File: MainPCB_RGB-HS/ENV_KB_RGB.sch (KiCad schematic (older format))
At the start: 297 parts

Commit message: Generated JLCPCB Compatible Gerber, BOM and CPL for HS/RGB Version
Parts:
- PowerLedResistor0: value 1K Resistor 0402 -> 2.2K Resistor 0402
- SW-RST0: value B3U-1000 -> B3U
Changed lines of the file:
@@
 P 8550 9950
 F 0 "PowerLedResistor0" V 8650 10200 50  0000 C CNN
-F 1 "1K Resistor 0402" V 8700 10000 50  0001 C CNN
+F 1 "2.2K Resistor 0402" V 8700 10000 50  0001 C CNN
 F 2 "Resistor_SMD:R_0402_1005Metric" H 8550 9950 50  0001 C CNN
 F 3 "~" H 8550 9950 50  0001 C CNN
@@
 P 8550 10700
 F 0 "SW-RST0" H 8550 11100 50  0000 C CNN
-F 1 "B3U-1000" H 8550 10950 50  0000 C CNN
+F 1 "B3U" H 8550 10950 50  0000 C CNN
 F 2 "Button_Switch_SMD:SW_SPST_B3U-1000P" H 8550 10700 50  0001 L BNN
 F 3 "" H 8550 10700 50  0001 L BNN

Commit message: shrunk the PCBs width down to 347mm to comply with JLCPCBs max size for 4 layers.
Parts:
- H0, H1, H10, H3, H4, H6, H7, H9: symbol Mechanical:MountingHole -> Mechanical:MountingHole_Pad
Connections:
- net GND: now also H0.1, H1.1, H10.1, H3.1, H4.1, H6.1, H7.1, H9.1
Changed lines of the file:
@@
 This needs double checking
 $Comp
-L Mechanical:MountingHole H9
+L Mechanical:MountingHole_Pad H9
 U 1 1 60717F95
 P 6600 10650
@@
 $EndComp
 $Comp
-L Mechanical:MountingHole H10
+L Mechanical:MountingHole_Pad H10
 U 1 1 607429B3
-P 6600 10850
-F 0 "H10" H 6700 10896 50  0000 L CNN
-F 1 "MountingHole" H 6700 10805 50  0000 L CNN
-F 2 "MountingHole:MountingHole_2.2mm_M2_Pad" H 6600 10850 50  0001 C CNN
-F 3 "~" H 6600 10850 50  0001 C CNN
-	1    6600 10850
+P 6800 10650
+F 0 "H10" H 6900 10696 50  0000 L CNN
+F 1 "MountingHole" H 6900 10605 50  0000 L CNN
+F 2 "MountingHole:MountingHole_2.2mm_M2_Pad" H 6800 10650 50  0001 C CNN
+F 3 "~" H 6800 10650 50  0001 C CNN
+	1    6800 10650
 	1    0    0    -1
 $EndComp
@@
 GND
 $Comp
-L Mechanical:MountingHole H7
+L Mechanical:MountingHole_Pad H7
 U 1 1 6077360A
-P 6600 10250
-F 0 "H7" H 6700 10296 50  0000 L CNN
-F 1 "MountingHole" H 6700 10205 50  0000 L CNN
-F 2 "MountingHole:MountingHole_2.2mm_M2_Pad" H 6600 10250 50  0001 C CNN
-F 3 "~" H 6600 10250 50  0001 C CNN
-	1    6600 10250
-	1    0    0    -1
-$EndComp
-$Comp
-L Mechanical:MountingHole H6
+P 6400 10650
+F 0 "H7" H 6500 10696 50  0000 L CNN
+F 1 "MountingHole" H 6500 10605 50  0000 L CNN
+F 2 "MountingHole:MountingHole_2.2mm_M2_Pad" H 6400 10650 50  0001 C CNN
+F 3 "~" H 6400 10650 50  0001 C CNN
+	1    6400 10650
+	1    0    0    -1
+$EndComp
+$Comp
+L Mechanical:MountingHole_Pad H6
 U 1 1 60748B43
-P 6600 10050
-F 0 "H6" H 6700 10096 50  0000 L CNN
-F 1 "MountingHole" H 6700 10005 50  0000 L CNN
-F 2 "MountingHole:MountingHole_2.2mm_M2_Pad" H 6600 10050 50  0001 C CNN
-F 3 "~" H 6600 10050 50  0001 C CNN
-	1    6600 10050
-	1    0    0    -1
-$EndComp
-$Comp
-L Mechanical:MountingHole H4
+P 6200 10650
+F 0 "H6" H 6300 10696 50  0000 L CNN
+F 1 "MountingHole" H 6300 10605 50  0000 L CNN
+F 2 "MountingHole:MountingHole_2.2mm_M2_Pad" H 6200 10650 50  0001 C CNN
+F 3 "~" H 6200 10650 50  0001 C CNN
+	1    6200 10650
+	1    0    0    -1
+$EndComp
+$Comp
+L Mechanical:MountingHole_Pad H4
 U 1 1 6068A680
-P 6600 9650
-F 0 "H4" H 6700 9696 50  0000 L CNN
-F 1 "MountingHole" H 6700 9605 50  0000 L CNN
-F 2 "MountingHole:MountingHole_2.2mm_M2_Pad" H 6600 9650 50  0001 C CNN
-F 3 "~" H 6600 9650 50  0001 C CNN
-	1    6600 9650
-	1    0    0    -1
-$EndComp
-$Comp
-L Mechanical:MountingHole H1
+P 6000 10650
+F 0 "H4" H 6100 10696 50  0000 L CNN
+F 1 "MountingHole" H 6100 10605 50  0000 L CNN
+F 2 "MountingHole:MountingHole_2.2mm_M2_Pad" H 6000 10650 50  0001 C CNN
+F 3 "~" H 6000 10650 50  0001 C CNN
+	1    6000 10650
+	1    0    0    -1
+$EndComp
+$Comp
+L Mechanical:MountingHole_Pad H1
 U 1 1 605BD366
-P 6600 9050
-F 0 "H1" H 6700 9096 50  0000 L CNN
-F 1 "MountingHole" H 6700 9005 50  0000 L CNN
-F 2 "MountingHole:MountingHole_2.2mm_M2_Pad" H 6600 9050 50  0001 C CNN
-F 3 "~" H 6600 9050 50  0001 C CNN
-	1    6600 9050
-	1    0    0    -1
-$EndComp
-$Comp
-L Mechanical:MountingHole H3
+P 5600 10650
+F 0 "H1" H 5700 10696 50  0000 L CNN
+F 1 "MountingHole" H 5700 10605 50  0000 L CNN
+F 2 "MountingHole:MountingHole_2.2mm_M2_Pad" H 5600 10650 50  0001 C CNN
+F 3 "~" H 5600 10650 50  0001 C CNN
+	1    5600 10650
+	1    0    0    -1
+$EndComp
+$Comp
+L Mechanical:MountingHole_Pad H3
 U 1 1 6058BC08
-P 6600 9450
-F 0 "H3" H 6700 9496 50  0000 L CNN
-F 1 "MountingHole" H 6700 9405 50  0000 L CNN
-F 2 "MountingHole:MountingHole_2.2mm_M2_Pad" H 6600 9450 50  0001 C CNN
-F 3 "~" H 6600 9450 50  0001 C CNN
-	1    6600 9450
-	1    0    0    -1
-$EndComp
-$Comp
-L Mechanical:MountingHole H0
+P 5800 10650
+F 0 "H3" H 5900 10696 50  0000 L CNN
+F 1 "MountingHole" H 5900 10605 50  0000 L CNN
+F 2 "MountingHole:MountingHole_2.2mm_M2_Pad" H 5800 10650 50  0001 C CNN
+F 3 "~" H 5800 10650 50  0001 C CNN
+	1    5800 10650
+	1    0    0    -1
+$EndComp
+$Comp
+L Mechanical:MountingHole_Pad H0
 U 1 1 605938C3
-P 6600 8850
-F 0 "H0" H 6700 8896 50  0000 L CNN
-F 1 "MountingHole" H 6700 8805 50  0000 L CNN
-F 2 "MountingHole:MountingHole_2.2mm_M2_Pad" H 6600 8850 50  0001 C CNN
-F 3 "~" H 6600 8850 50  0001 C CNN
-	1    6600 8850
+P 5400 10650
+F 0 "H0" H 5500 10696 50  0000 L CNN
+F 1 "MountingHole" H 5500 10605 50  0000 L CNN
+F 2 "MountingHole:MountingHole_2.2mm_M2_Pad" H 5400 10650 50  0001 C CNN
+F 3 "~" H 5400 10650 50  0001 C CNN
+	1    5400 10650
 	1    0    0    -1
 $EndComp
@@
 Wire Wire Line
 	30200 3500 30250 3500
+Wire Wire Line
+	5400 10750 5600 10750
+Connection ~ 5600 10750
+Wire Wire Line
+	5600 10750 5800 10750
+Connection ~ 5800 10750
+Wire Wire Line
+	5800 10750 6000 10750
+Connection ~ 6000 10750
+Wire Wire Line
+	6000 10750 6200 10750
+Connection ~ 6200 10750
+Wire Wire Line
+	6200 10750 6400 10750
+Connection ~ 6400 10750
+Wire Wire Line
+	6400 10750 6600 10750
+Connection ~ 6600 10750
+Wire Wire Line
+	6600 10750 6800 10750
+Wire Wire Line
+	6800 10750 6800 11000
+Connection ~ 6800 10750
+Text GLabel 6800 11000 2    50   Input ~ 0
+GND
 $EndSCHEMATC

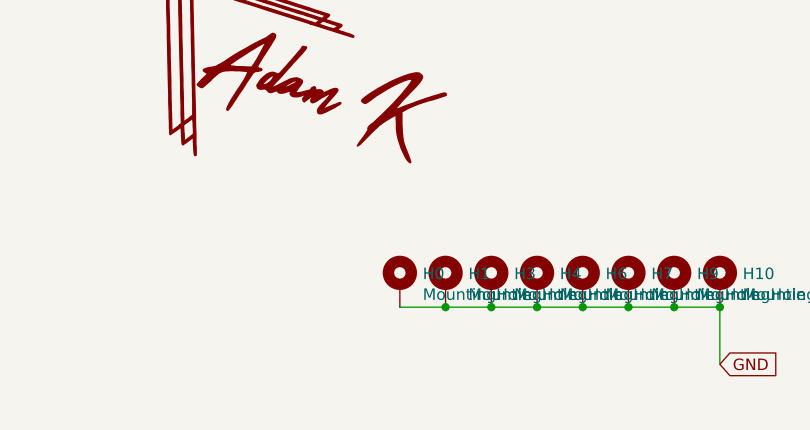
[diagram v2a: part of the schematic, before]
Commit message: Modified RGB/HS to be less wide so you can have it made via JLCPCB, Also made new logo and name for this version.
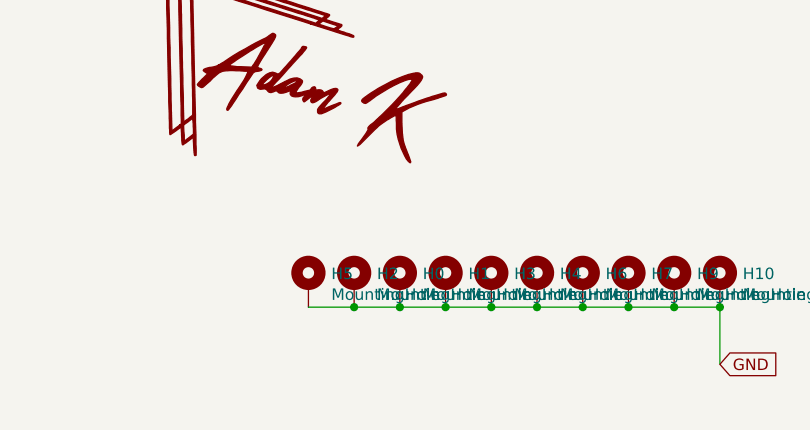
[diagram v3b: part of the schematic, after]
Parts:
- added H2, H5: MountingHole, MountingHole:MountingHole_2.2mm_M2_Pad, symbol Mechanical:MountingHole_Pad
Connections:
- net GND: now also H2.1, H5.1
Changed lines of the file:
@@
 Text GLabel 6800 11000 2    50   Input ~ 0
 GND
+$Comp
+L Mechanical:MountingHole_Pad H2
+U 1 1 61411D60
+P 5200 10650
+F 0 "H2" H 5300 10696 50  0000 L CNN
+F 1 "MountingHole" H 5300 10605 50  0000 L CNN
+F 2 "MountingHole:MountingHole_2.2mm_M2_Pad" H 5200 10650 50  0001 C CNN
+F 3 "~" H 5200 10650 50  0001 C CNN
+	1    5200 10650
+	1    0    0    -1
+$EndComp
+Wire Wire Line
+	5200 10750 5400 10750
+Connection ~ 5400 10750
+$Comp
+L Mechanical:MountingHole_Pad H5
+U 1 1 6162A1BF
+P 5000 10650
+F 0 "H5" H 5100 10696 50  0000 L CNN
+F 1 "MountingHole" H 5100 10605 50  0000 L CNN
+F 2 "MountingHole:MountingHole_2.2mm_M2_Pad" H 5000 10650 50  0001 C CNN
+F 3 "~" H 5000 10650 50  0001 C CNN
+	1    5000 10650
+	1    0    0    -1
+$EndComp
+Wire Wire Line
+	5000 10750 5200 10750
+Connection ~ 5200 10750
 $EndSCHEMATC

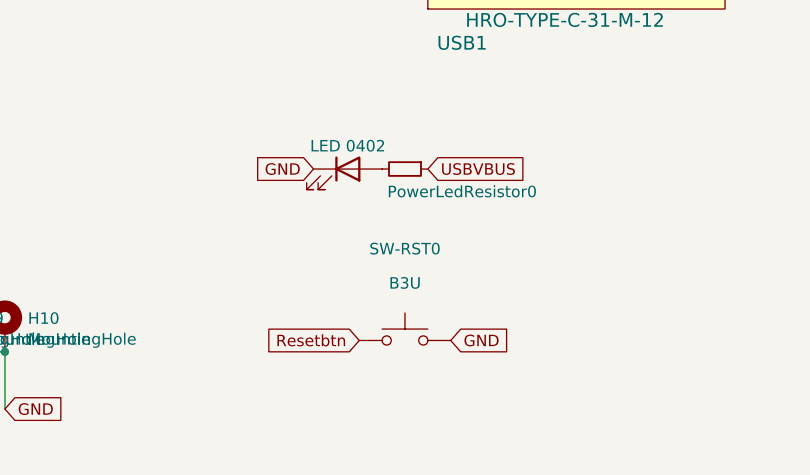
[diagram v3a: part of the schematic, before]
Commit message: updated PCB to have through hole parts except type-c port.
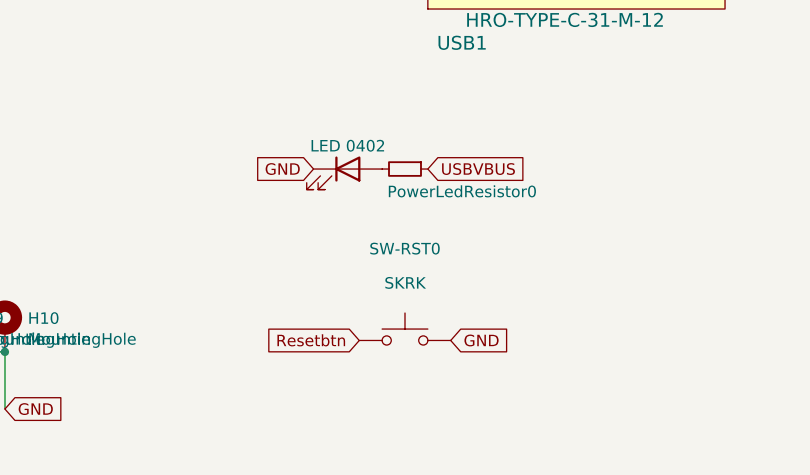
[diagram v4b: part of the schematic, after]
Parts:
- PowerLED0: footprint LED_SMD:LED_0402_1005Metric -> LED_THT:LED_D3.0mm
- PowerLedResistor0, RESISTOR0, RESISTOR1: footprint Resistor_SMD:R_0402_1005Metric -> Resistor_THT:R_Axial_DIN0204_L3.6mm_D1.6mm_P5.08mm_Horizontal
- SW-RST0: value B3U -> SKRK; footprint Button_Switch_SMD:SW_SPST_B3U-1000P -> Button_Switch_SMD:SW_Push_SPST_NO_Alps_SKRK
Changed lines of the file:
@@
 F 0 "RESISTOR1" V 8804 8600 39  0001 C CNN
 F 1 "5.1kohm 0402" V 9000 8700 30  0001 C CNN
-F 2 "Resistor_SMD:R_0402_1005Metric" H 9000 8600 50  0001 C CNN
+F 2 "Resistor_THT:R_Axial_DIN0204_L3.6mm_D1.6mm_P5.08mm_Horizontal" H 9000 8600 50  0001 C CNN
 F 3 "~" H 9000 8600 50  0001 C CNN
 F 4 "C25905" V 9000 8600 50  0001 C CNN "LCSC"
@@
 F 0 "RESISTOR0" V 9404 8600 39  0001 C CNN
 F 1 "5.1kohm 0402" V 9495 8600 50  0001 C CNN
-F 2 "Resistor_SMD:R_0402_1005Metric" H 9600 8600 50  0001 C CNN
+F 2 "Resistor_THT:R_Axial_DIN0204_L3.6mm_D1.6mm_P5.08mm_Horizontal" H 9600 8600 50  0001 C CNN
 F 3 "~" H 9600 8600 50  0001 C CNN
 F 4 "C25905" V 9600 8600 50  0001 C CNN "LCSC"
@@
 F 0 "PowerLED0" H 8293 10167 50  0001 C CNN
 F 1 "LED 0402" H 8300 10050 50  0000 C CNN
-F 2 "LED_SMD:LED_0402_1005Metric" H 8300 9950 50  0001 C CNN
+F 2 "LED_THT:LED_D3.0mm" H 8300 9950 50  0001 C CNN
 F 3 "~" H 8300 9950 50  0001 C CNN
 	1    8300 9950
@@
 F 0 "PowerLedResistor0" V 8650 10200 50  0000 C CNN
 F 1 "2.2K Resistor 0402" V 8700 10000 50  0001 C CNN
-F 2 "Resistor_SMD:R_0402_1005Metric" H 8550 9950 50  0001 C CNN
+F 2 "Resistor_THT:R_Axial_DIN0204_L3.6mm_D1.6mm_P5.08mm_Horizontal" H 8550 9950 50  0001 C CNN
 F 3 "~" H 8550 9950 50  0001 C CNN
 F 4 "C17513" V 8550 9950 50  0001 C CNN "LCSC"
@@
 P 8550 10700
 F 0 "SW-RST0" H 8550 11100 50  0000 C CNN
-F 1 "B3U" H 8550 10950 50  0000 C CNN
-F 2 "Button_Switch_SMD:SW_SPST_B3U-1000P" H 8550 10700 50  0001 L BNN
+F 1 "SKRK" H 8550 10950 50  0000 C CNN
+F 2 "Button_Switch_SMD:SW_Push_SPST_NO_Alps_SKRK" H 8550 10700 50  0001 L BNN
 F 3 "" H 8550 10700 50  0001 L BNN
 F 4 "Omron" H 8550 10700 50  0001 L BNN "MANUFACTURER"

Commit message: some more general re-working of HS/RGB version
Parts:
- added Stab1: Stabilizer, Mounting_Keyboard_Stabilizer:Stabilizer_Cherry_MX_6.25u, symbol Mechanical:MountingHole
- added Stab2, Stab3, Stab4: Stabilizer, Mounting_Keyboard_Stabilizer:Stabilizer_Cherry_MX_2u, symbol Mechanical:MountingHole
- K_0, K_1, K_10, K_11, K_12, K_13, K_14, K_15, K_16, K_17, K_18, K_19, K_2, K_20, K_21, K_22, K_23, K_24, K_25, K_26, K_27, K_28, K_3, K_30, K_31, K_32, K_34, K_35, K_36, K_37, K_38, K_39, K_4, K_40, K_41, K_42, K_43, K_44, K_45, K_47, K_48, K_49, K_5, K_51, K_52, K_53, K_54, K_55, K_56, K_57, K_58, K_59, K_6, K_60, K_61, K_62, K_65, K_66, K_67, K_68, K_69, K_7, K_70, K_71, K_72, K_73, K_74, K_75, K_77, K_8, K_86, K_87, K_88, K_9: footprint MX_Only:MXOnly-1U-Hotswap -> MX_Only:MXOnly-1U-Hotswap-Modified
- K_29, K_63: footprint MX_Only:MXOnly-2U-Hotswap -> MX_Only:MXOnly-1U-Hotswap-Modified
- K_33, K_46: footprint MX_Only:MXOnly-1.5U-Hotswap -> MX_Only:MXOnly-1U-Hotswap-Modified
- K_50: footprint MX_Only:MXOnly-1.75U-Hotswap -> MX_Only:MXOnly-1U-Hotswap-Modified
- K_63B1, K_64B1: footprint MX_Only:MXOnly-2.25U-Hotswap -> MX_Only:MXOnly-1U-Hotswap-Modified
- K_64, K_78, K_79, K_80, K_82, K_83, K_84, K_85: footprint MX_Only:MXOnly-1.25U-Hotswap -> MX_Only:MXOnly-1U-Hotswap-Modified
- K_76: footprint MX_Only:MXOnly-2.75U-Hotswap -> MX_Only:MXOnly-1U-Hotswap-Modified
- K_81: footprint MX_Only:MXOnly-6.25U-Hotswap-ReversedStabilizers -> MX_Only:MXOnly-1U-Hotswap-Modified

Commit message: generated laser cut files for current PCB version, changed footprint size of resistors to 1/4 instead of 1/8w
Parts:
- LEDRESISTOR1: renamed from PowerLedResistor0; value 2.2K Resistor 0402 -> 5.1K Resistor 1/4w; footprint Resistor_THT:R_Axial_DIN0204_L3.6mm_D1.6mm_P5.08mm_Horizontal -> Resistor_THT:R_Axial_DIN0204_L3.6mm_D1.6mm_P7.62mm_Horizontal
- PowerLED0: value LED 0402 -> LED 3MM
- RESISTOR0: value 5.1kohm 0402 -> 5.1kohm 1/4w; footprint Resistor_THT:R_Axial_DIN0204_L3.6mm_D1.6mm_P5.08mm_Horizontal -> Resistor_THT:R_Axial_DIN0204_L3.6mm_D1.6mm_P7.62mm_Horizontal
- RESISTOR1: value 5.1kohm 0402 -> 5.1kohm 1/4; footprint Resistor_THT:R_Axial_DIN0204_L3.6mm_D1.6mm_P5.08mm_Horizontal -> Resistor_THT:R_Axial_DIN0204_L3.6mm_D1.6mm_P7.62mm_Horizontal
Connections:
- no-connect marks 0 -> 2
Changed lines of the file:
@@
 P 9000 8600
 F 0 "RESISTOR1" V 8804 8600 39  0001 C CNN
-F 1 "5.1kohm 0402" V 9000 8700 30  0001 C CNN
-F 2 "Resistor_THT:R_Axial_DIN0204_L3.6mm_D1.6mm_P5.08mm_Horizontal" H 9000 8600 50  0001 C CNN
+F 1 "5.1kohm 1/4" V 9000 8700 30  0001 C CNN
+F 2 "Resistor_THT:R_Axial_DIN0204_L3.6mm_D1.6mm_P7.62mm_Horizontal" H 9000 8600 50  0001 C CNN
 F 3 "~" H 9000 8600 50  0001 C CNN
 F 4 "C25905" V 9000 8600 50  0001 C CNN "LCSC"
@@
 P 9600 8600
 F 0 "RESISTOR0" V 9404 8600 39  0001 C CNN
-F 1 "5.1kohm 0402" V 9495 8600 50  0001 C CNN
-F 2 "Resistor_THT:R_Axial_DIN0204_L3.6mm_D1.6mm_P5.08mm_Horizontal" H 9600 8600 50  0001 C CNN
+F 1 "5.1kohm 1/4w" V 9495 8600 50  0001 C CNN
+F 2 "Resistor_THT:R_Axial_DIN0204_L3.6mm_D1.6mm_P7.62mm_Horizontal" H 9600 8600 50  0001 C CNN
 F 3 "~" H 9600 8600 50  0001 C CNN
 F 4 "C25905" V 9600 8600 50  0001 C CNN "LCSC"
@@
 P 8300 9950
 F 0 "PowerLED0" H 8293 10167 50  0001 C CNN
-F 1 "LED 0402" H 8300 10050 50  0000 C CNN
+F 1 "LED 3MM" H 8300 10050 50  0000 C CNN
 F 2 "LED_THT:LED_D3.0mm" H 8300 9950 50  0001 C CNN
 F 3 "~" H 8300 9950 50  0001 C CNN
@@
 USBVBUS
 $Comp
-L Device:R_Small PowerLedResistor0
+L Device:R_Small LEDRESISTOR1
 U 1 1 604A80B1
 P 8550 9950
-F 0 "PowerLedResistor0" V 8650 10200 50  0000 C CNN
-F 1 "2.2K Resistor 0402" V 8700 10000 50  0001 C CNN
-F 2 "Resistor_THT:R_Axial_DIN0204_L3.6mm_D1.6mm_P5.08mm_Horizontal" H 8550 9950 50  0001 C CNN
+F 0 "LEDRESISTOR1" V 8650 10200 50  0000 C CNN
+F 1 "5.1K Resistor 1/4w" V 8700 10000 50  0001 C CNN
+F 2 "Resistor_THT:R_Axial_DIN0204_L3.6mm_D1.6mm_P7.62mm_Horizontal" H 8550 9950 50  0001 C CNN
 F 3 "~" H 8550 9950 50  0001 C CNN
 F 4 "C17513" V 8550 9950 50  0001 C CNN "LCSC"
@@
 	1    0    0    1
 $EndComp
+NoConn ~ 8900 8700
+NoConn ~ 9500 8700
 $EndSCHEMATC

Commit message: Corrected resistor footprint and adjusted placement, added cutout for direct mount usb castellation.
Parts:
- LEDRESISTOR1, RESISTOR0, RESISTOR1: footprint Resistor_THT:R_Axial_DIN0204_L3.6mm_D1.6mm_P7.62mm_Horizontal -> Resistor_THT:R_Axial_DIN0207_L6.3mm_D2.5mm_P10.16mm_Horizontal
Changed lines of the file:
@@
 F 0 "RESISTOR1" V 8804 8600 39  0001 C CNN
 F 1 "5.1kohm 1/4" V 9000 8700 30  0001 C CNN
-F 2 "Resistor_THT:R_Axial_DIN0204_L3.6mm_D1.6mm_P7.62mm_Horizontal" H 9000 8600 50  0001 C CNN
+F 2 "Resistor_THT:R_Axial_DIN0207_L6.3mm_D2.5mm_P10.16mm_Horizontal" H 9000 8600 50  0001 C CNN
 F 3 "~" H 9000 8600 50  0001 C CNN
 F 4 "C25905" V 9000 8600 50  0001 C CNN "LCSC"
@@
 F 0 "RESISTOR0" V 9404 8600 39  0001 C CNN
 F 1 "5.1kohm 1/4w" V 9495 8600 50  0001 C CNN
-F 2 "Resistor_THT:R_Axial_DIN0204_L3.6mm_D1.6mm_P7.62mm_Horizontal" H 9600 8600 50  0001 C CNN
+F 2 "Resistor_THT:R_Axial_DIN0207_L6.3mm_D2.5mm_P10.16mm_Horizontal" H 9600 8600 50  0001 C CNN
 F 3 "~" H 9600 8600 50  0001 C CNN
 F 4 "C25905" V 9600 8600 50  0001 C CNN "LCSC"
@@
 F 0 "LEDRESISTOR1" V 8650 10200 50  0000 C CNN
 F 1 "5.1K Resistor 1/4w" V 8700 10000 50  0001 C CNN
-F 2 "Resistor_THT:R_Axial_DIN0204_L3.6mm_D1.6mm_P7.62mm_Horizontal" H 8550 9950 50  0001 C CNN
+F 2 "Resistor_THT:R_Axial_DIN0207_L6.3mm_D2.5mm_P10.16mm_Horizontal" H 8550 9950 50  0001 C CNN
 F 3 "~" H 8550 9950 50  0001 C CNN
 F 4 "C17513" V 8550 9950 50  0001 C CNN "LCSC"

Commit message: Generated updated gerbers.
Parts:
- PowerLED0: footprint LED_THT:LED_D3.0mm -> LED_THT:LED_D3.0mm_FlatTop
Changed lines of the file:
@@
 F 0 "PowerLED0" H 8293 10167 50  0001 C CNN
 F 1 "LED 3MM" H 8300 10050 50  0000 C CNN
-F 2 "LED_THT:LED_D3.0mm" H 8300 9950 50  0001 C CNN
+F 2 "LED_THT:LED_D3.0mm_FlatTop" H 8300 9950 50  0001 C CNN
 F 3 "~" H 8300 9950 50  0001 C CNN
 	1    8300 9950
